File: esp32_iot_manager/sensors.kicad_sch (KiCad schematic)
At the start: 0 parts

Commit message: sensor and user interface done
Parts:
- added C16, C17, C18, C20: 0.1u, Capacitor_SMD:C_0805_2012Metric, symbol PCM_SL_Devices:Capacitor_NP
- added MK1: CMC-5042PF-AC, CMC-5042PF-AC:CUI_CMC-5042PF-AC, symbol CMC-5042PF-AC:CMC-5042PF-AC
- added Q1: TEMT6000X01, TEMT6000X01:TRANS_TEMT6000X01, symbol TEMT6000X01:TEMT6000X01
- added R14, R27: 1M, Resistor_SMD:R_0805_2012Metric, symbol PCM_SL_Resistors:Resistor
- added R23: 10K, Resistor_SMD:R_0805_2012Metric, symbol Device:R
- added R24, R25: 4.7K, Resistor_SMD:R_0805_2012Metric, symbol Device:R
- added R26, R28: 2K, Resistor_SMD:R_0805_2012Metric, symbol PCM_SL_Resistors:Resistor
- added R30: 10K, Resistor_SMD:R_0805_2012Metric, symbol PCM_SL_Resistors:Resistor
- added R31: 100K, Resistor_SMD:R_0805_2012Metric, symbol PCM_SL_Resistors:Resistor
- added U2: BME280, BME280:PSON65P250X250X100-8N, symbol BME280:BME280
- added U7: MAX4466EXK, MAX4466EXK:SOT65P210X110-5N, symbol MAX4466EXK:MAX4466EXK
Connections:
- new net: MK1.OUT, R14.2, R27.1, R28.1, U7.1 (IN+)
- new net: C17.1, R26.1, R28.2
- new net 3.3V: C16.2, C18.2, R23.1, R24.1, R25.1, R26.2, R27.2, U2.2 (CSB), U2.6 (VDDIO), U2.8 (VDD), U7.5 (VCC)
- new net GND: C16.1, C17.2, C18.1, C20.1, MK1.GND, Q1.1, R14.1, R30.1, R30.2, R31.1, U2.1 (GND), U2.5 (SDO), U2.7 (GND), U7.2 (GND), U7.3 (IN-)
- new net MIC_OUT: C20.2, R31.2, U7.4 (OUT)
- new net PHOTO_C: Q1.3, R23.2
- new net SCL: R24.2, U2.4 (SCK)
- new net SDA: R25.2, U2.3 (SDI)
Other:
- note added: "Digital environmental sensor"
- note added: "Microphone and amplifier"
- note added: "Photo sensor"
- title: (none) -> Sensors and microphone

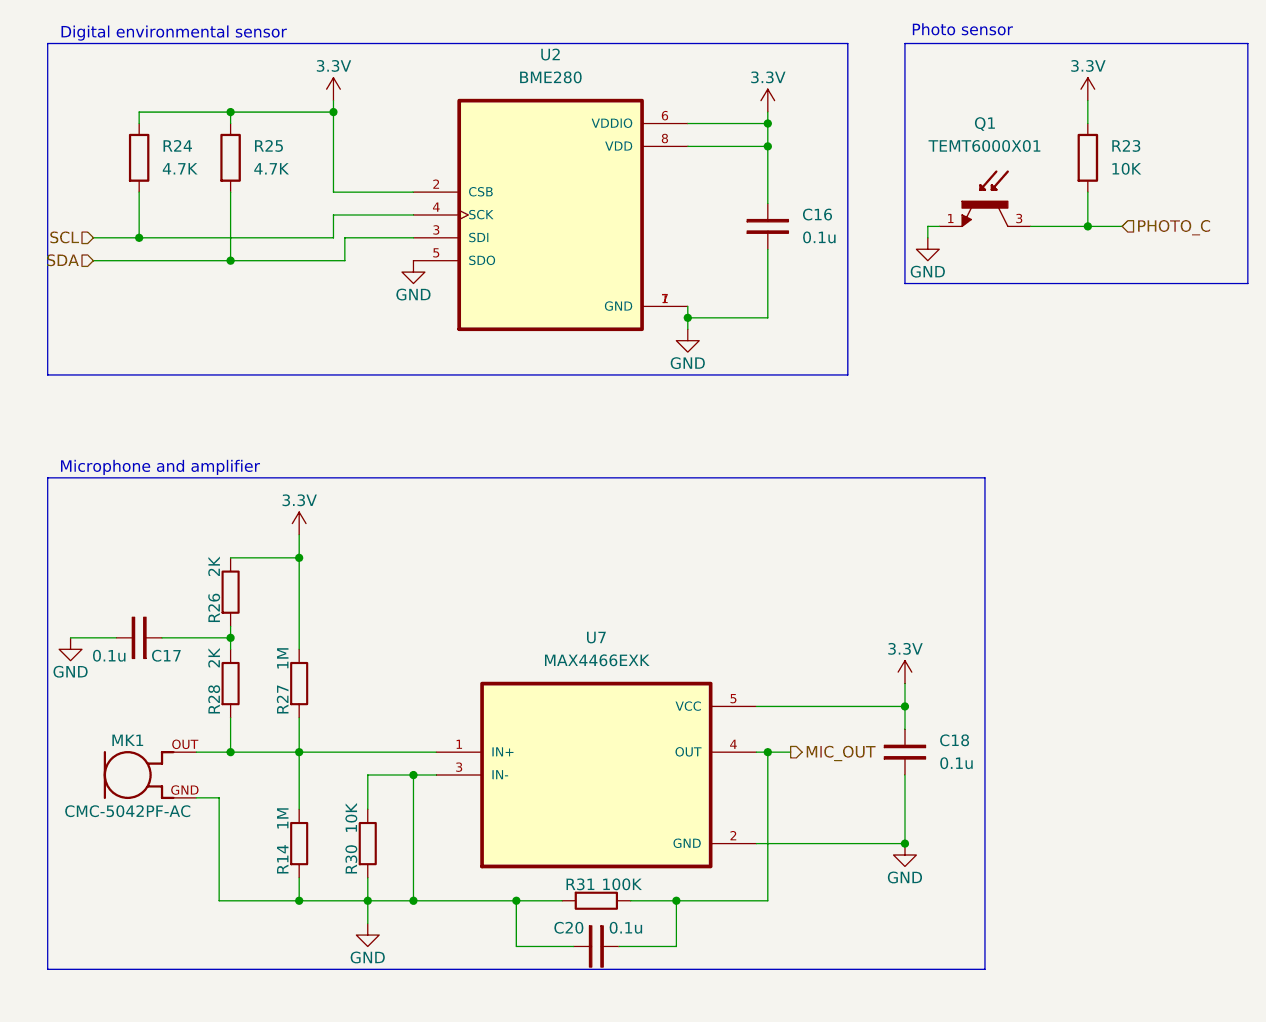
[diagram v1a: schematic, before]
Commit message: finished design of pcb, next copper zones, routing
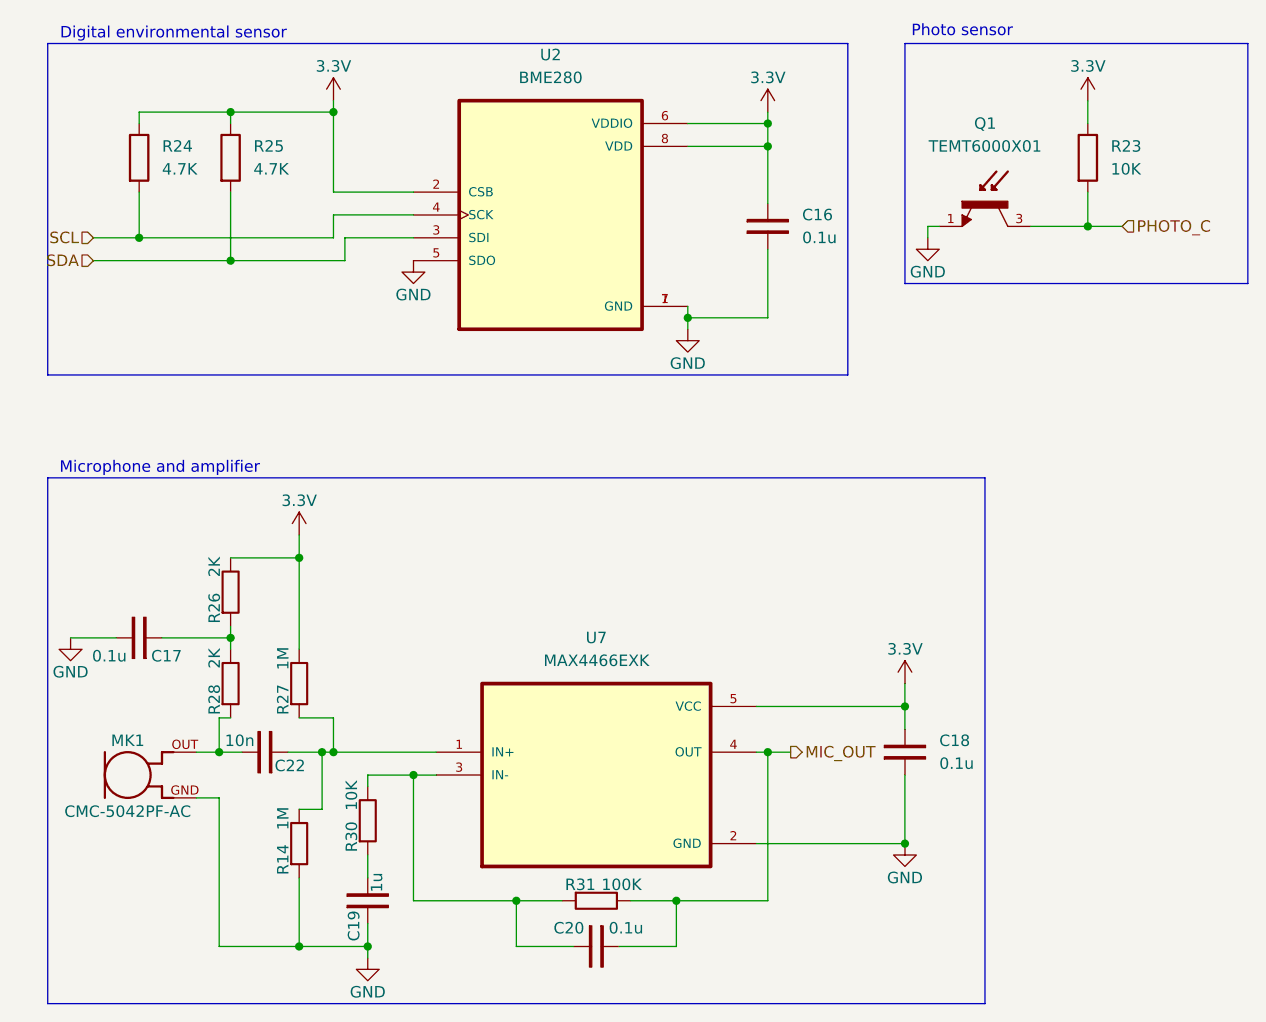
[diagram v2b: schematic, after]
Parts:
- added C19: 1u, Capacitor_SMD:C_0805_2012Metric, symbol PCM_SL_Devices:Capacitor_NP
- added C22: 10n, Capacitor_SMD:C_0805_2012Metric, symbol PCM_SL_Devices:Capacitor_NP
- MK1: footprint CMC-5042PF-AC:CUI_CMC-5042PF-AC -> esp32_manager_project:CUI_CMC-5042PF-AC
- Q1: footprint TEMT6000X01:TRANS_TEMT6000X01 -> esp32_manager_project:TRANS_TEMT6000X01
- U2: footprint BME280:PSON65P250X250X100-8N -> esp32_manager_project:PSON65P250X250X100-8N
- U7: footprint MAX4466EXK:SOT65P210X110-5N -> esp32_manager_project:SOT65P210X110-5N
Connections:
- net GND: now also C19.1; no longer C20.1, R30.1, R30.2, R31.1, U7.3 (IN-)
- net at R14.2, R27.1, U7.1 (IN+): now also C22.1; no longer MK1.OUT, R28.1
- new net: C22.2, MK1.OUT, R28.1
- new net: C20.1, R30.2, R31.1, U7.3 (IN-)
- new net: C19.2, R30.1
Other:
- moved on the sheet: R30
